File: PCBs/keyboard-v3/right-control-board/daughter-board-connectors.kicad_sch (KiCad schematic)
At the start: 12 parts, among them J601 F31Z1A7H111008, J602 F31Z1A7H111008, U601 NCP380HMU05AATBG, U602 NCP380HMU05AATBG

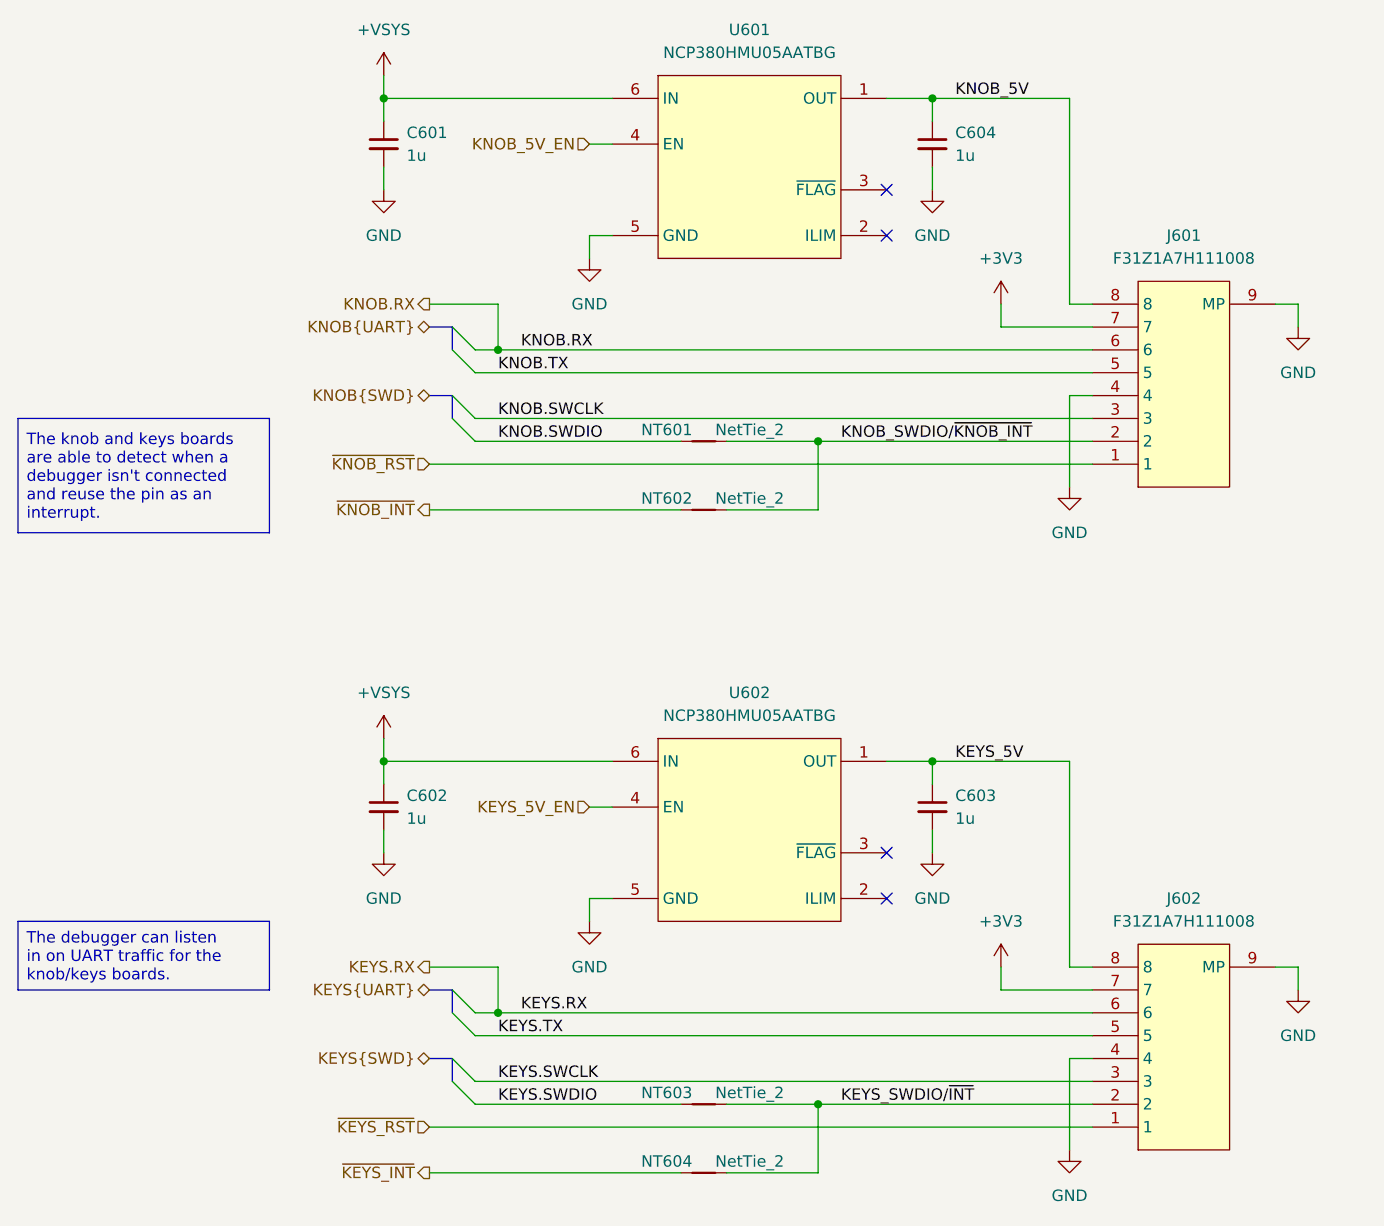
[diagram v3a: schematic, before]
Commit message: Added mounting holes
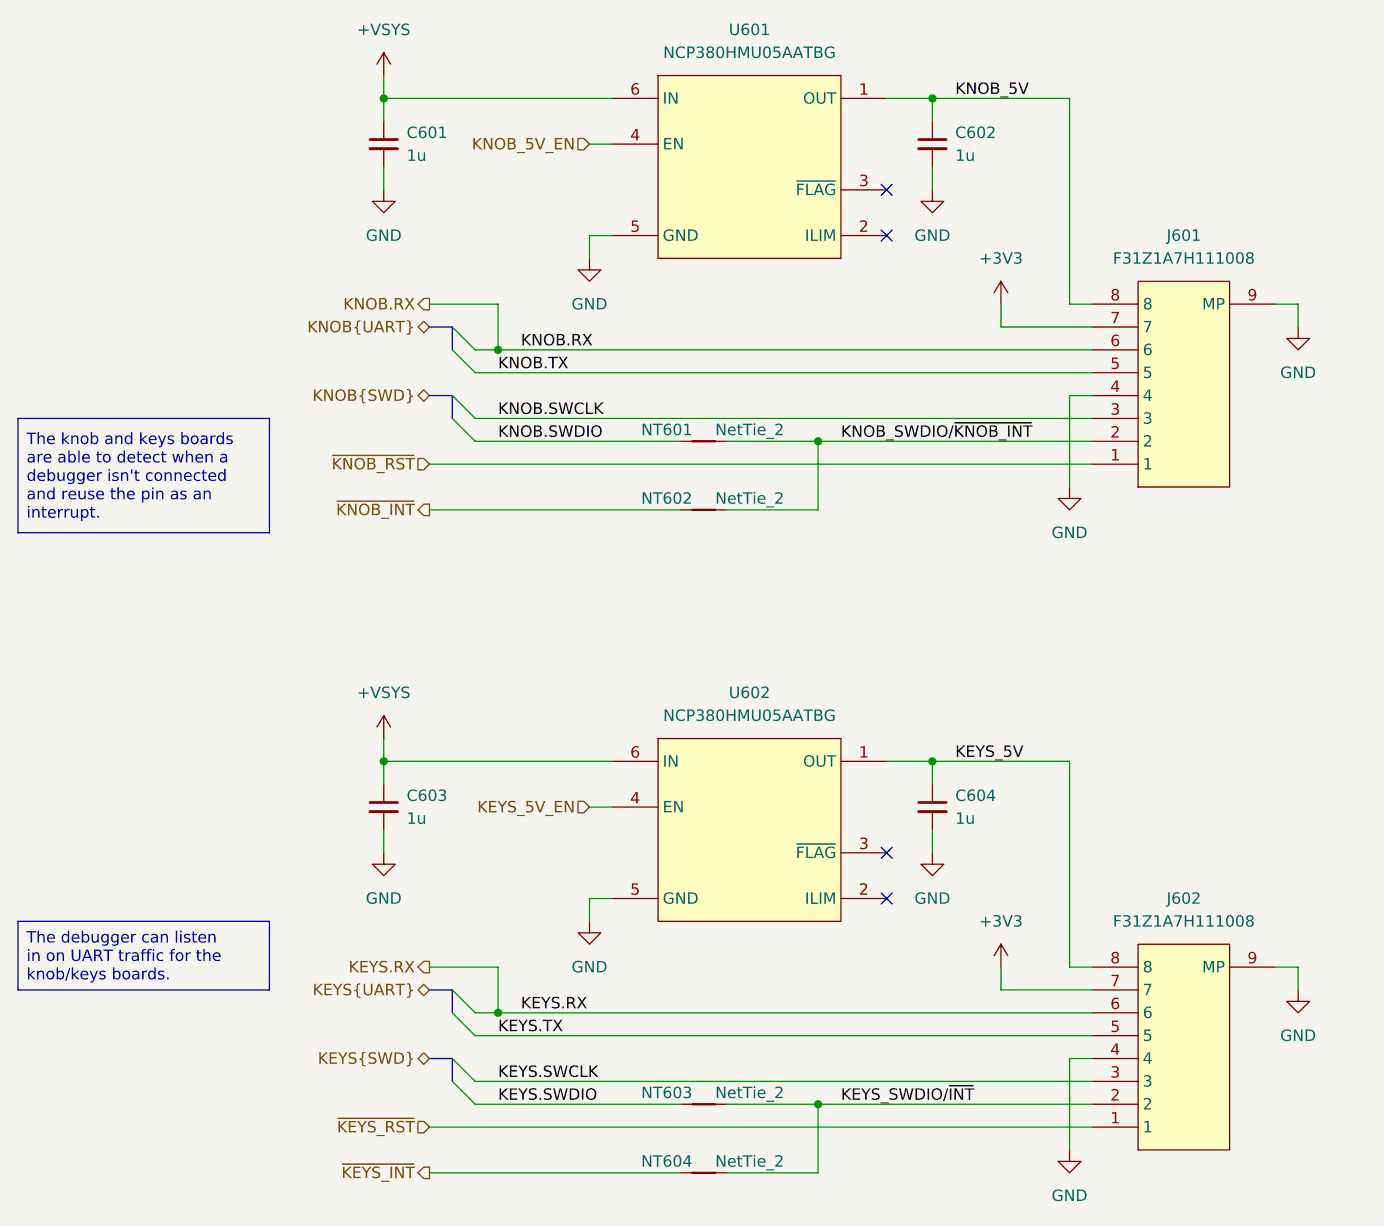
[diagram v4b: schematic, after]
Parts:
- renumbered C604 to C602, C602 to C603, C603 to C604
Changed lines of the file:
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@@
 		(dnp no)
 		(fields_autoplaced yes)
-		(property "Reference" "#PWR0614"
+		(property "Reference" "#PWR0603"
 			(at 172.72 52.07 0)
 			(effects
@@
 			(project "right-control-board"
 				(path "/982f1c46-f6d6-42a2-bf2a-9fb0e913f11f/5e632e5a-5283-4d2d-96d4-75c4ba68d1b5"
-					(reference "#PWR0614")
+					(reference "#PWR0603")
 					(unit 1)
 				)
@@
 		(dnp no)
 		(fields_autoplaced yes)
-		(property "Reference" "#PWR0610"
+		(property "Reference" "#PWR0608"
 			(at 111.76 110.49 0)
 			(effects
@@
 			(project "right-control-board"
 				(path "/982f1c46-f6d6-42a2-bf2a-9fb0e913f11f/5e632e5a-5283-4d2d-96d4-75c4ba68d1b5"
-					(reference "#PWR0610")
+					(reference "#PWR0608")
 					(unit 1)
 				)
@@
 		(dnp no)
 		(fields_autoplaced yes)
-		(property "Reference" "#PWR0613"
+		(property "Reference" "#PWR0610"
 			(at 172.72 125.73 0)
 			(effects
@@
 			(project "right-control-board"
 				(path "/982f1c46-f6d6-42a2-bf2a-9fb0e913f11f/5e632e5a-5283-4d2d-96d4-75c4ba68d1b5"
-					(reference "#PWR0613")
+					(reference "#PWR0610")
 					(unit 1)
 				)
@@
 		(dnp no)
 		(fields_autoplaced yes)
-		(property "Reference" "C602"
+		(property "Reference" "C603"
 			(at 114.3 113.0362 0)
 			(effects
@@
 			(project "right-control-board"
 				(path "/982f1c46-f6d6-42a2-bf2a-9fb0e913f11f/5e632e5a-5283-4d2d-96d4-75c4ba68d1b5"
-					(reference "C602")
+					(reference "C603")
 					(unit 1)
 				)
@@
 		(dnp no)
 		(fields_autoplaced yes)
-		(property "Reference" "#PWR0611"
+		(property "Reference" "#PWR0609"
 			(at 111.76 125.73 0)
 			(effects
@@
 			(project "right-control-board"
 				(path "/982f1c46-f6d6-42a2-bf2a-9fb0e913f11f/5e632e5a-5283-4d2d-96d4-75c4ba68d1b5"
-					(reference "#PWR0611")
+					(reference "#PWR0609")
 					(unit 1)
 				)
@@
 		(dnp no)
 		(fields_autoplaced yes)
-		(property "Reference" "#PWR0603"
+		(property "Reference" "#PWR0606"
 			(at 213.36 67.31 0)
 			(effects
@@
 			(project "right-control-board"
 				(path "/982f1c46-f6d6-42a2-bf2a-9fb0e913f11f/5e632e5a-5283-4d2d-96d4-75c4ba68d1b5"
-					(reference "#PWR0603")
+					(reference "#PWR0606")
 					(unit 1)
 				)
@@
 		(dnp no)
 		(fields_autoplaced yes)
-		(property "Reference" "#PWR0604"
+		(property "Reference" "#PWR0614"
 			(at 187.96 158.75 0)
 			(effects
@@
 			(project "right-control-board"
 				(path "/982f1c46-f6d6-42a2-bf2a-9fb0e913f11f/5e632e5a-5283-4d2d-96d4-75c4ba68d1b5"
-					(reference "#PWR0604")
+					(reference "#PWR0614")
 					(unit 1)
 				)
@@
 		(dnp no)
 		(fields_autoplaced yes)
-		(property "Reference" "#PWR0612"
+		(property "Reference" "#PWR0611"
 			(at 134.62 133.35 0)
 			(effects
@@
 			(project "right-control-board"
 				(path "/982f1c46-f6d6-42a2-bf2a-9fb0e913f11f/5e632e5a-5283-4d2d-96d4-75c4ba68d1b5"
-					(reference "#PWR0612")
+					(reference "#PWR0611")
 					(unit 1)
 				)
@@
 		(dnp no)
 		(fields_autoplaced yes)
-		(property "Reference" "#PWR0606"
+		(property "Reference" "#PWR0607"
 			(at 187.96 85.09 0)
 			(effects
@@
 			(project "right-control-board"
 				(path "/982f1c46-f6d6-42a2-bf2a-9fb0e913f11f/5e632e5a-5283-4d2d-96d4-75c4ba68d1b5"
-					(reference "#PWR0606")
+					(reference "#PWR0607")
 					(unit 1)
 				)
@@
 		(dnp no)
 		(fields_autoplaced yes)
-		(property "Reference" "#PWR0608"
+		(property "Reference" "#PWR0604"
 			(at 134.62 59.69 0)
 			(effects
@@
 			(project "right-control-board"
 				(path "/982f1c46-f6d6-42a2-bf2a-9fb0e913f11f/5e632e5a-5283-4d2d-96d4-75c4ba68d1b5"
-					(reference "#PWR0608")
+					(reference "#PWR0604")
 					(unit 1)
 				)
@@
 		(dnp no)
 		(fields_autoplaced yes)
-		(property "Reference" "C604"
+		(property "Reference" "C602"
 			(at 175.26 39.3762 0)
 			(effects
@@
 			(project "right-control-board"
 				(path "/982f1c46-f6d6-42a2-bf2a-9fb0e913f11f/5e632e5a-5283-4d2d-96d4-75c4ba68d1b5"
-					(reference "C604")
+					(reference "C602")
 					(unit 1)
 				)
@@
 		(dnp no)
 		(fields_autoplaced yes)
-		(property "Reference" "#PWR0609"
+		(property "Reference" "#PWR0602"
 			(at 111.76 52.07 0)
 			(effects
@@
 			(project "right-control-board"
 				(path "/982f1c46-f6d6-42a2-bf2a-9fb0e913f11f/5e632e5a-5283-4d2d-96d4-75c4ba68d1b5"
-					(reference "#PWR0609")
+					(reference "#PWR0602")
 					(unit 1)
 				)
@@
 		(dnp no)
 		(fields_autoplaced yes)
-		(property "Reference" "C603"
+		(property "Reference" "C604"
 			(at 175.26 113.0362 0)
 			(effects
@@
 			(project "right-control-board"
 				(path "/982f1c46-f6d6-42a2-bf2a-9fb0e913f11f/5e632e5a-5283-4d2d-96d4-75c4ba68d1b5"
-					(reference "C603")
+					(reference "C604")
 					(unit 1)
 				)
@@
 		(dnp no)
 		(fields_autoplaced yes)
-		(property "Reference" "#PWR0607"
+		(property "Reference" "#PWR0612"
 			(at 180.34 135.89 0)
 			(effects
@@
 			(project "right-control-board"
 				(path "/982f1c46-f6d6-42a2-bf2a-9fb0e913f11f/5e632e5a-5283-4d2d-96d4-75c4ba68d1b5"
-					(reference "#PWR0607")
+					(reference "#PWR0612")
 					(unit 1)
 				)
@@
 		(dnp no)
 		(fields_autoplaced yes)
-		(property "Reference" "#PWR0602"
+		(property "Reference" "#PWR0613"
 			(at 213.36 140.97 0)
 			(effects
@@
 			(project "right-control-board"
 				(path "/982f1c46-f6d6-42a2-bf2a-9fb0e913f11f/5e632e5a-5283-4d2d-96d4-75c4ba68d1b5"
-					(reference "#PWR0602")
-					(unit 1)
-				)
+					(reference "#PWR0613")
+					(unit 1)
+				)
